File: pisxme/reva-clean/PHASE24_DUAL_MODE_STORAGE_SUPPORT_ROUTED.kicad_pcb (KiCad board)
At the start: 6 copper layers, 300 x 180 mm, 117 parts, among them J1 74221-101LF, J2 A70-112-331N126, J3 1-2199230-4, J4 Amphenol 10171746-00021LF USB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, J5 0039300020, J6 0039300020, J7 Raspberry-Pi-5-Compute-Module, Q1 CSD19536KCS, Q2 CSD19536KCS, U1 LM74700QDBVRQ1, U2 LM74700QDBVRQ1, U3 TPSM63606RDLR, U4 TPSM63606RDLR, U5 TPSM63606RDLR, U6 TPD4EUSB30, U7 TUSB9261IPVP, U8 Texas_DRT_3, U9 TPD4EUSB30, Y10 25MHz

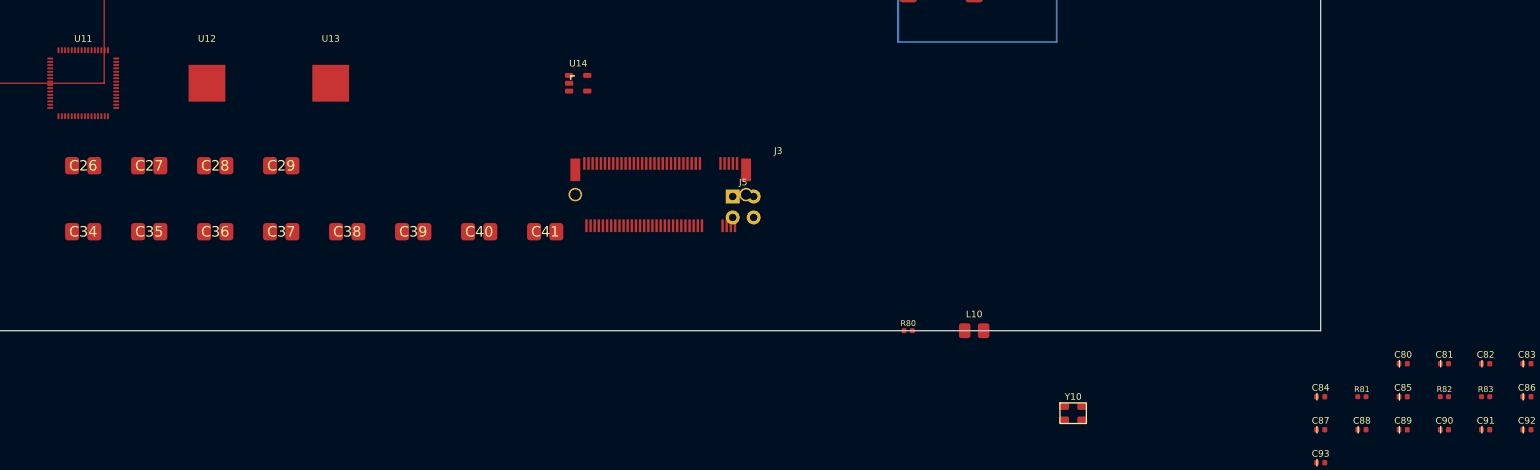
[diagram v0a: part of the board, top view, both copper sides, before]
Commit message: phase24 route initial JMS583 support fixture
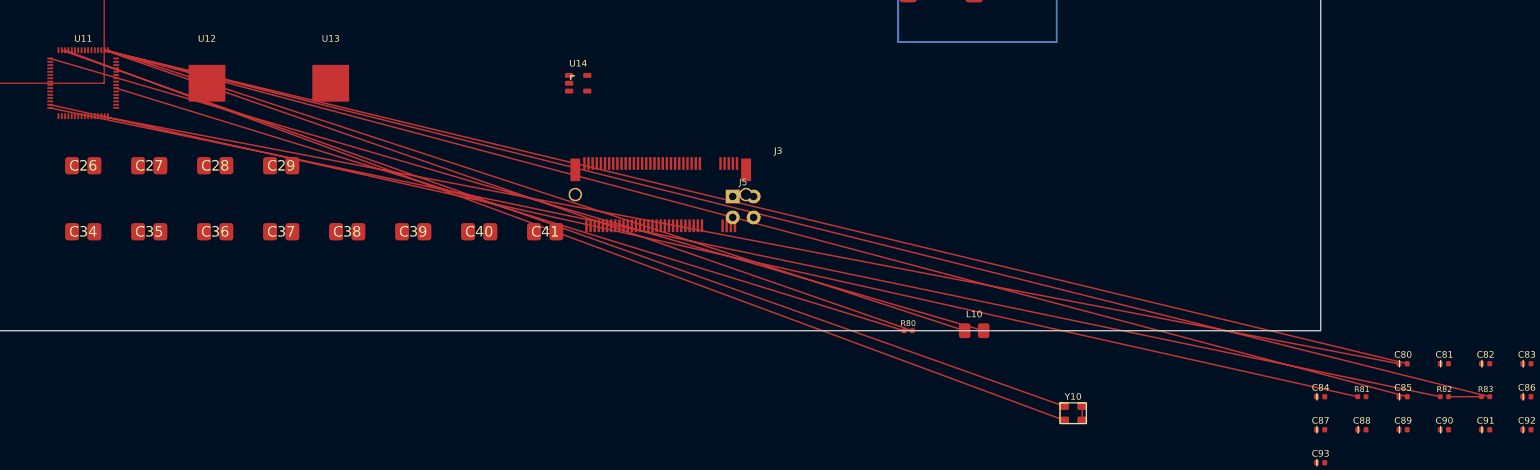
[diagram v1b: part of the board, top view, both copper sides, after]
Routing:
- net POWER_GND: track 173.5 -> 777.7 mm
- net VBUS: track 0.00 -> 172.1 mm
- net JMS_RESET_N: track 0.00 -> 162.4 mm
- net JMS_AVDD33: track 0.00 -> 160.1 mm
- net JMS_XOUT: track 0.00 -> 129.1 mm
- net JMS_XIN: track 0.00 -> 128.9 mm
- net JMS_VDDREG_5V: track 0.00 -> 117.9 mm
- net JMS_LXO: track 0.00 -> 109.3 mm
- net JMS_REXT: track 0.00 -> 99.9 mm
- net JMS_VBUS_SENSE: track 0.00 -> 4.00 mm
